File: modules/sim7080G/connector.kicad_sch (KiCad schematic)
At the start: 5 parts, among them J1 Bus_M.2_Socket_E

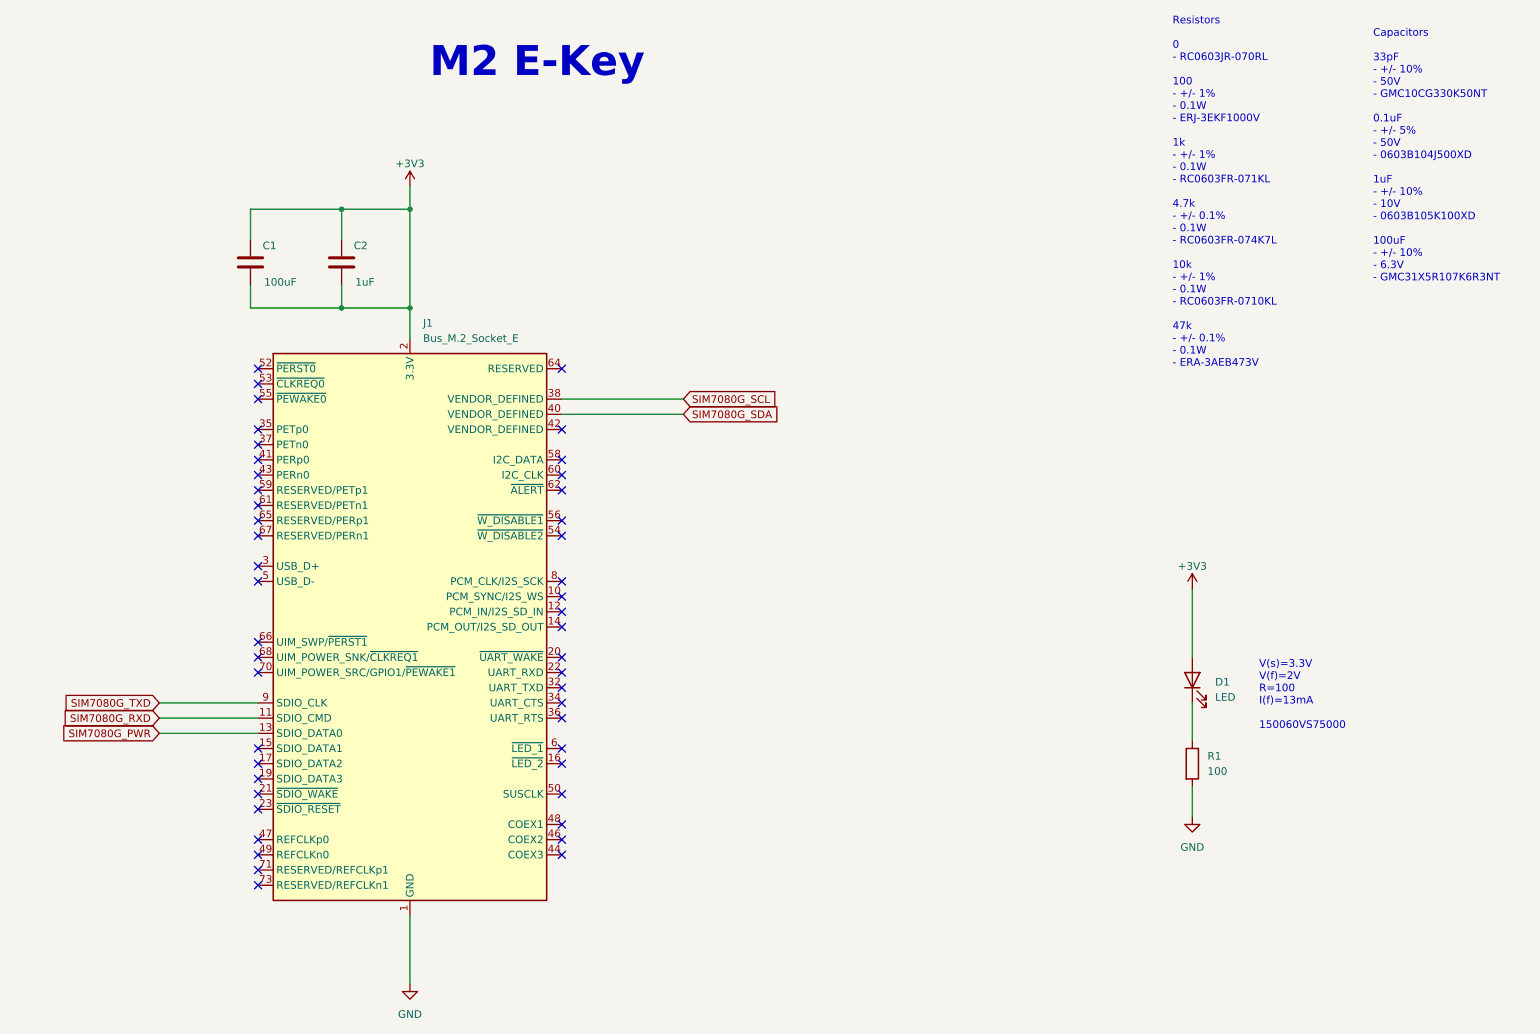
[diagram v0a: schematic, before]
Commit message: fix: remodify board to be a baseboard
Signed-off-by: Rodney Osodo <socials@rodneyosodo.com>
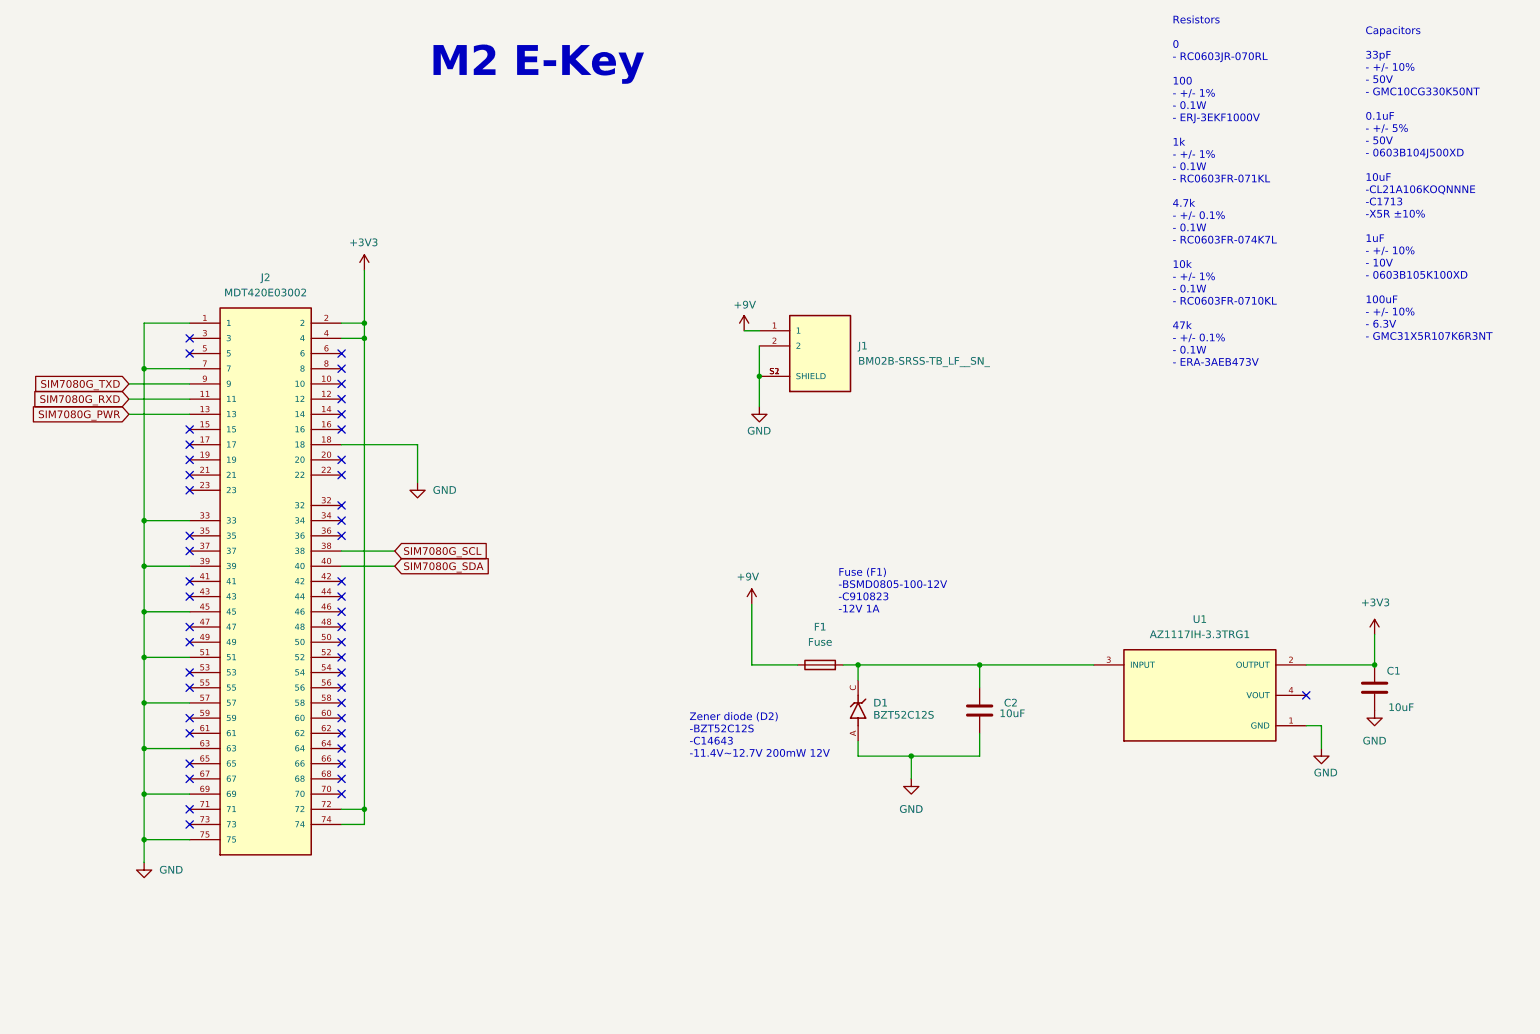
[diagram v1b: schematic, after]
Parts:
- removed D1: LED, LED_SMD:LED_0603_1608Metric, symbol Device:LED
- removed J1: Bus_M.2_Socket_E, M.2-Key-E-Footprints-master:2242-key-E, symbol Connector:Bus_M.2_Socket_E
- removed R1: 100, Resistor_SMD:R_0603_1608Metric, symbol Device:R
- added D1: BZT52C12S, BZT52C12S:DIO_BZT52C12S, symbol BZT52C12S:BZT52C12S
- added F1: Fuse, Fuse:Fuse_0402_1005Metric_Pad0.77x0.64mm_HandSolder, symbol Device:Fuse
- added J1: BM02B-SRSS-TB_LF__SN_, BM02B-SRSS-TB_LF__SN_:JST_BM02B-SRSS-TB_LF__SN_, symbol BM02B-SRSS-TB_LF__SN_:BM02B-SRSS-TB_LF__SN_
- added J2: MDT420E03002, MDT420E03002:AMPHENOL_MDT420E03002, symbol MDT420E03002:MDT420E03002
- added U1: AZ1117IH-3.3TRG1, AZ1117IH-3.3TRG1:SOT230P700X185-4N, symbol AZ1117IH-3.3TRG1:AZ1117IH-3.3TRG1
- C1: value 100uF -> 10uF
- C2: value 1uF -> 10uF; footprint Capacitor_SMD:C_0603_1608Metric -> Capacitor_SMD:C_1206_3216Metric
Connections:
- net +3V3: now also J2.2, J2.4, J2.72, J2.74, U1.2 (OUTPUT); no longer C1.2, C2.1, C2.2
- net GND: now also C1.2, C2.2, D1.A, J1.2, J1.S1 (SHIELD), J1.S2 (SHIELD), J2.1, J2.18, J2.33, J2.39, J2.45, J2.51, J2.57, J2.63, J2.69, J2.7, J2.75, U1.1 (GND)
- net SIM7080G_PWR: now also J2.13
- net SIM7080G_RXD: now also J2.11
- net SIM7080G_SCL: now also J2.38
- net SIM7080G_SDA: now also J2.40
- net SIM7080G_TXD: now also J2.9
- new net: C2.1, D1.C, F1.2, U1.3 (INPUT)
- new net +9V: F1.1, J1.1
- no-connect marks 47 -> 48
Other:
- note added: "Capacitors 33pF - +/- 10% - 50V - GMC10CG330K50NT 0.1uF - +/- 5% - 50V - 0603B104J500XD 10uF -CL21A106KOQNNNE -C1713 -X5R ±10% 1uF - +/- 10% - 10V - 0603B105K100XD 100uF - +/- 10% - 6.3V - GMC31X5R107K6R3NT"
- note added: "Fuse (F1) -BSMD0805-100-12V -C910823 -12V 1A"
- note added: "Zener diode (D2) -BZT52C12S -C14643 -11.4V~12.7V 200mW 12V"
- note removed: "Capacitors 33pF - +/- 10% - 50V - GMC10CG330K50NT 0.1uF - +/- 5% - 50V - 0603B104J500XD 1uF - +/- 10% - 10V - 0603B105K100XD 100uF - +/- 10% - 6.3V - GMC31X5R107K6R3NT"
- note removed: "V(s)=3.3V V(f)=2V R=100 I(f)=13mA 150060VS75000"
